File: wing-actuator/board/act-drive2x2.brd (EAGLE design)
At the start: 133.6 x 78.7 mm, 104 parts, among them J1 POWER_JACKPTH_LOCK, Q1 BSS123, Q2 BSS123, U5 Q50-5C, U7 LP2985-33, U8 TPS62160, X1 SMA-142-0701-801/806, X2 SMA-142-0701-801/806, X3 SMA-142-0701-801/806, X4 SMA-142-0701-801/806, X5 2516-

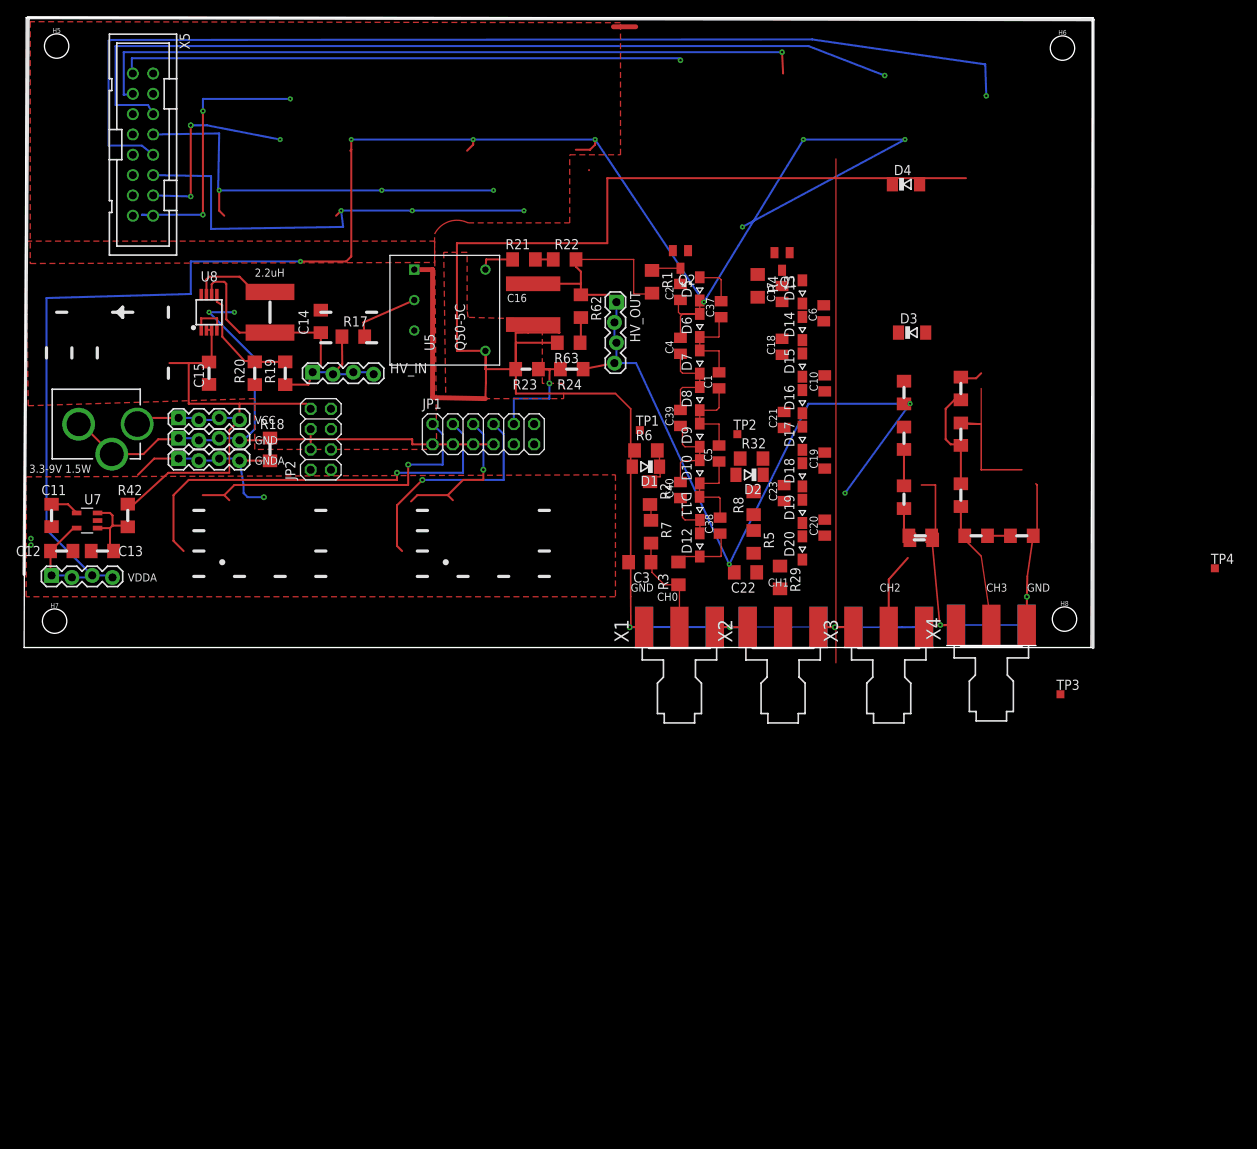
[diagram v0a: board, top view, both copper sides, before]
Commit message: adding 2x2 array
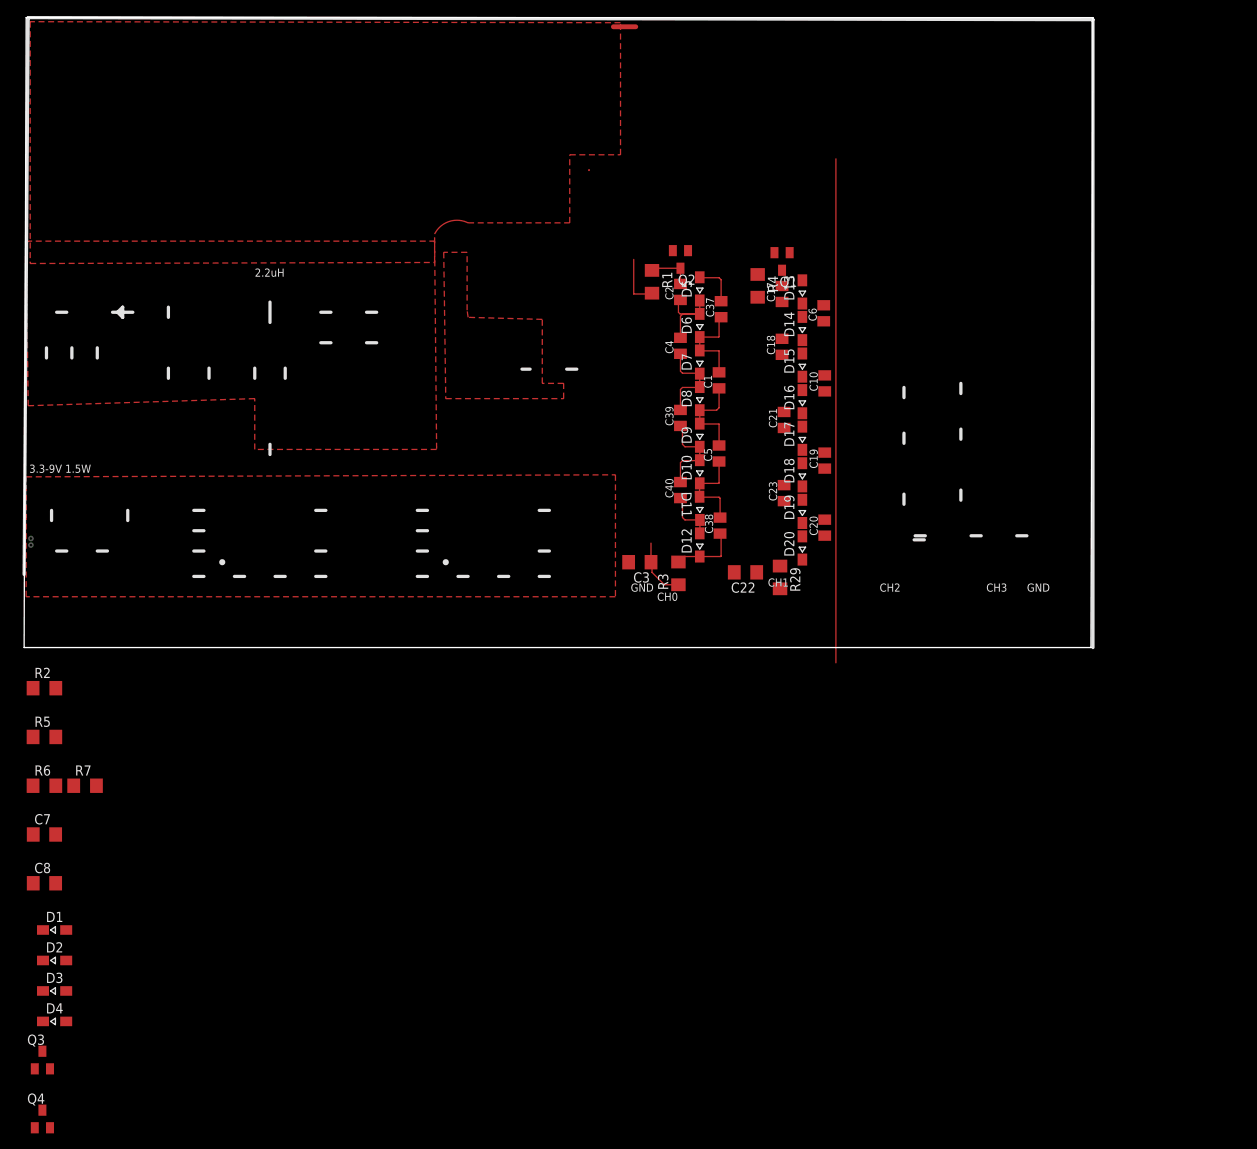
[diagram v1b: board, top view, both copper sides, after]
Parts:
- removed C11: 10nF, rcl:C1206
- removed C12, C13: 2.2uF, rcl:C1206
- removed C14, C15: 22uF, rcl:C1206
- removed C16: 100nF-1k5V, rcl:C2225K
- removed C29, C34: 1nF 1k5V, rcl:C1206
- removed GND, GNDA, HV_IN, HV_OUT, VCC, VDDA: (no value), modular_robotics:1X04_LOCK
- removed H5, H6, H7, H8: STAND-OFFTIGHT, SparkFun-Hardware:STAND-OFF-TIGHT
- removed J1: POWER_JACKPTH_LOCK, SparkFun-Connectors:POWER_JACK_PTH_LOCK
- removed JP1: (no value), pinhead:2X06
- removed JP2: (no value), pinhead:2X04
- removed L1: 2.2uH, modular_robotics:SRN6045
- removed R17: FUSE, rcl:R1206
- removed R18: 0R, rcl:R1206
- removed R19, R21, R22: 510k, rcl:R1206
- removed R20: 100k, rcl:R1206
- removed R23: 270k, rcl:R1206
- removed R24: 100M, rcl:R1206
- removed R32, R60: 22k, rcl:R1206
- removed R42: FERRITE, rcl:R1206
- removed R46: 1M, rcl:R1206
- removed R47, R50, R56, R59, R8: 5M, rcl:R1206
- removed R51: 22K, rcl:R1206
- removed R55, R62, R63: 10M, rcl:R1206
- removed TP1, TP2, TP3, TP4: TPTP10SQ, testpad:TP10SQ
- removed U$18: INFO, modular_robotics:INFO
- removed U5: Q50-5C, modular_robotics:Q50-5C
- removed U7: LP2985-33, modular_robotics:SOT23-5
- removed U8: TPS62160, modular_robotics:TSSOP8
- removed X1, X2, X3, X4: SMA-142-0701-801/806, con-coax:J502-ND-142-0701-801/806
- removed X5: 2516-, con-3m:PAK100/2500-16
- added C7: 1nF-1k5V, rcl:C1206
- added C8: 1nF 1k5V, rcl:C1206
- added Q3, Q4: BSS123, transistor-small-signal:SOT23
- D1, D2, D3, D4: value 3.0V -> (none); device diode:SOD80C -> diode:SOD323-W
- R2, R5, R7: value 5M -> 1M
- R6: value 22k -> 1M
- moved D4 149.3 mm to (3.56, -46.7)
- moved D3 135.1 mm to (3.56, -42.9)
- moved D2 106.0 mm to (3.56, -39.1), turned to 0 degrees
- moved D1 93.9 mm to (3.56, -35.3), turned to 0 degrees
- moved R5 91.9 mm to (2.29, -11.2), turned to 0 degrees
- moved R6 86.1 mm to (2.29, -17.3)
- moved R2 79.5 mm to (2.29, -5.08), turned to 0 degrees
- moved R7 77.5 mm to (7.37, -17.3), turned to 0 degrees
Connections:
- removed net GNDA: C11.2, C12.2, C13.2, GNDA.1, GNDA.2, GNDA.3, GNDA.4, R18.2, U7.2
- removed net HV_SENSE: JP1.10, R23.1, R24.2
- removed net ID0: D1.C, R2.1, R6.2, TP1.TP
- removed net ID1: D2.C, R32.2, R8.1, TP2.TP
- removed net ID2: D3.C, R50.1, R51.2, TP3.TP
- removed net ID3: D4.C, R59.1, R60.2, TP4.TP
- removed net I_SENSE_0: JP1.4
- removed net I_SENSE_1: JP1.8
- removed net N$20: R19.2, R20.2, U8.5
- removed net N$24: R21.1, R22.1
- removed net N$25: R47.2, R50.2
- removed net N$26: R55.1
- removed net N$27: R56.2, R59.2
- removed net N$37: C13.1, R42.2, U7.1, U7.3
- removed net N$60: R21.2, U5.3
- removed net N$62: R62.2, R63.1
- removed net PWM_0: Q2.1, X5.14
- removed net PWM_1: Q1.1, X5.16
- removed net PWM_2: X5.8
- removed net PWM_3: X5.12
- removed net SD_0: X5.1
- removed net SD_1: X5.3
- removed net SD_2: X5.6
- removed net SD_3: X5.10
- removed net VCC: C15.1, J1.PWR, JP2.8, R42.1, U8.2, U8.3, VCC.1, VCC.2, VCC.3, VCC.4
- removed net VDDA: C12.1, U7.5, VDDA.1, VDDA.2, VDDA.3, VDDA.4
- removed net VO2: C29.1, R46.2, R47.1, X3.1
- removed net VO3: C34.1, R55.2, R56.1, X4.1
- removed net V_SENSE_0: JP1.2
- removed net V_SENSE_1: JP1.6
- new net COL0: Q3.1
- new net COL1: Q4.1
- new net ROW0: Q2.1
- new net ROW1: Q1.1
- net GND: now also Q3.2, Q4.2; no longer C14.2, C15.2, C16.2, C22.2, C29.2, C3.2, C34.2, D1.A, D2.A, D3.A, D4.A, GND.1, GND.2, GND.3, GND.4, J1.GND, J1.GNDBREAK, JP1.1, JP1.3, JP1.5, JP1.7, JP2.4, JP2.6, R18.1, R20.1, R23.2, R32.1, R51.1, R6.1, R60.1, R63.2, U5.1, U5.4, U8.1, U8.4, X1.G@1, X1.G@2, X1.G@3, X1.G@4, X2.G@1, X2.G@2, X2.G@3, X2.G@4, X3.G@1, X3.G@2, X3.G@3, X3.G@4, X4.G@1, X4.G@2, X4.G@3, X4.G@4
- net N$12: now also C7.2, D2.A, R6.1; no longer R17.2, U5.2
- net N$17: now also C8.2, D4.A, R7.1; no longer L1.1, U8.7
- net N$18: now also D1.C, D3.C, Q3.3; no longer C14.1, HV_IN.1, HV_IN.2, HV_IN.3, HV_IN.4, L1.2, R17.1, R19.1, U8.6
- net N$19: now also D2.C, D4.C, Q4.3; no longer C11.1, U7.4
- net N$4: now also C3.2, D1.A, R2.1; no longer R2.2, R7.1
- net N$6: now also C22.2, D3.A; no longer R8.2
- net V+: no longer C16.1, HV_OUT.1, HV_OUT.2, HV_OUT.3, HV_OUT.4, R22.2, R24.1, R62.1
- net VO0: now also C7.1, R2.2, R6.2; no longer R7.2, X1.1
- net VO1: now also C8.1, R7.2; no longer X2.1
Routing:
- net GND: track 420.6 -> 8.29 mm, vias 7 -> 0
- net VDDA: track 229.3 -> 0.00 mm, vias 8 -> 0
- net SD_3: track 132.8 -> 0.00 mm, vias 1 -> 0
- net V+: track 120.6 -> 6.65 mm, vias 3 -> 0
- net SD_2: track 109.6 -> 0.00 mm, vias 1 -> 0
- net SD_1: track 91.5 -> 0.00 mm, vias 1 -> 0
- net SD_0: track 71.0 -> 0.00 mm, vias 1 -> 0
- net VCC: track 67.3 -> 0.00 mm
- net PWM_3: track 56.3 -> 0.00 mm, vias 3 -> 0
- net PWM_2: track 53.1 -> 0.00 mm, vias 3 -> 0
- net I_SENSE_0: track 52.0 -> 0.00 mm, vias 1 -> 0
- net N$18: track 48.1 -> 0.00 mm
- net V_SENSE_0: track 39.6 -> 0.00 mm, vias 1 -> 0
- net PWM_1: track 34.4 -> 0.00 mm, vias 3 -> 0
- net I_SENSE_1: track 28.1 -> 0.00 mm, vias 1 -> 0
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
